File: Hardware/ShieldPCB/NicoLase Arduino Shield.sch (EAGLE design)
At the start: 17 parts, among them IC1 4050D, J1 ARDUINO_R3_SHIELD, U1 7432SE

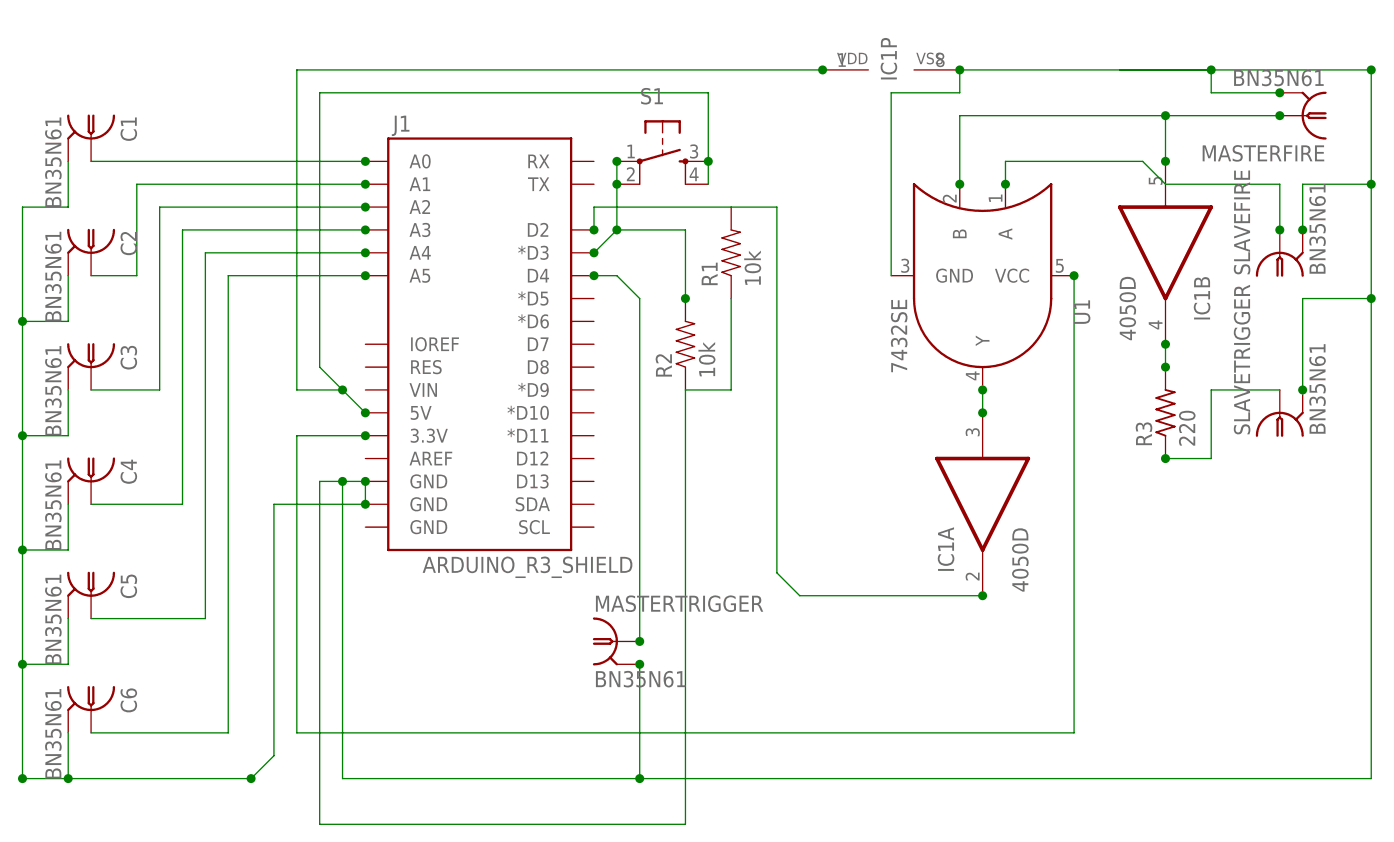
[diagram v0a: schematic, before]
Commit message: Updated PCB to include pull-down resistors on both inputs of OR gate.
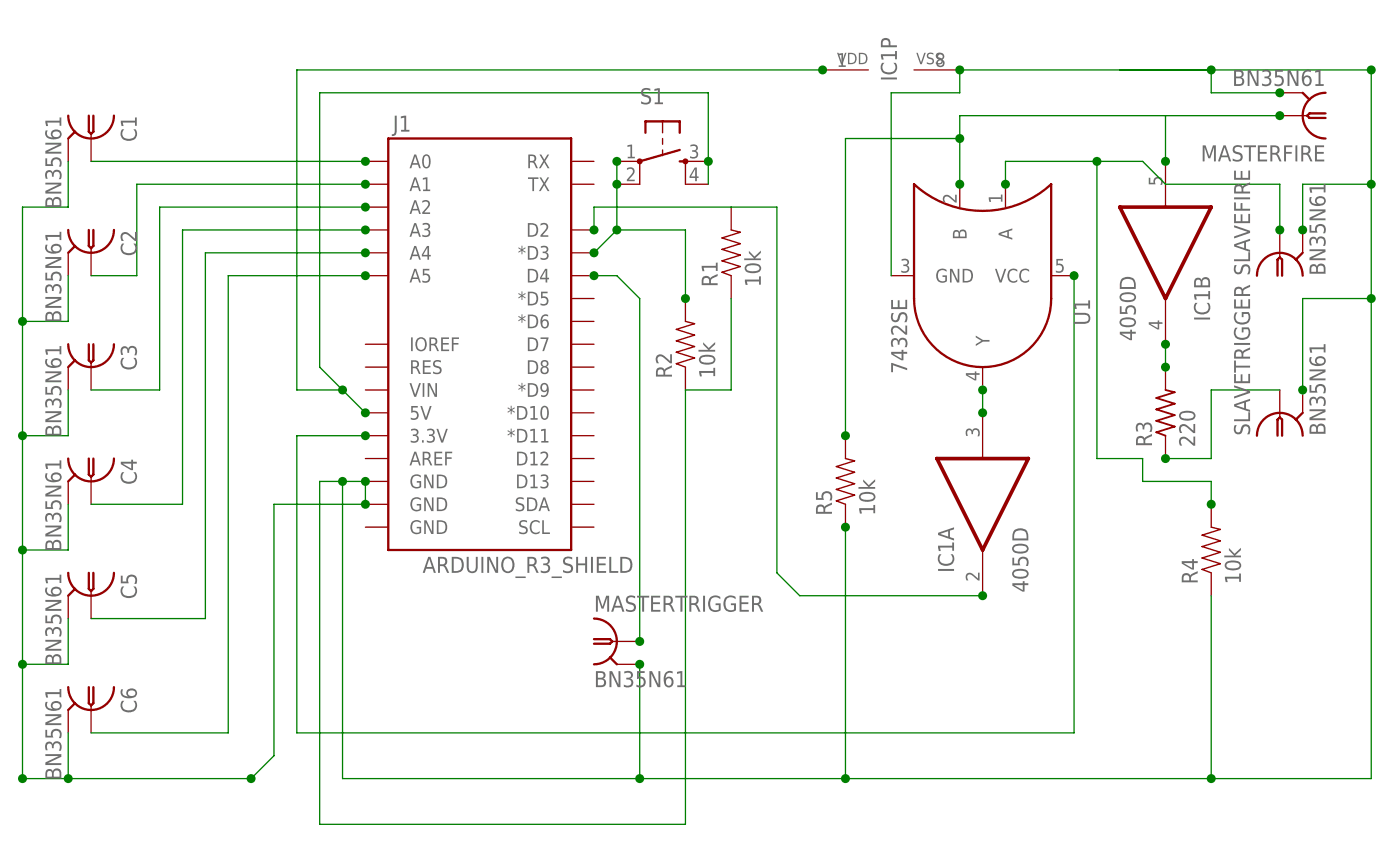
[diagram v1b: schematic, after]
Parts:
- added R4, R5: 10k, SparkFun-Resistors:RESISTOR1206
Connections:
- removed net N$14: SLAVEFIRE.1, U1.A
- new net N$26: R4.2, SLAVEFIRE.1, U1.A
- net N$2: now also R4.1, R5.1
- net SLAVEFIRE: now also R5.2
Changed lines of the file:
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@@
 <part name="MASTERTRIGGER" library="con-coax" deviceset="BN35N61" device=""/>
 <part name="J1" library="SparkFun-Boards" deviceset="ARDUINO_R3_SHIELD" device=""/>
+<part name="R4" library="SparkFun-Resistors" deviceset="RESISTOR" device="1206" value="10k"/>
+<part name="R5" library="SparkFun-Resistors" deviceset="RESISTOR" device="1206" value="10k"/>
 </parts>
 <sheets>
@@
 <instance part="MASTERTRIGGER" gate="G$1" x="76.2" y="27.94"/>
 <instance part="J1" gate="G$1" x="60.96" y="63.5"/>
+<instance part="R4" gate="G$1" x="142.24" y="38.1" rot="R90"/>
+<instance part="R5" gate="G$1" x="101.6" y="45.72" rot="R90"/>
 </instances>
 <busses>
@@
 <net name="SLAVEFIRE" class="0">
 <segment>
+<pinref part="U1" gate="G$1" pin="B"/>
+<wire x1="137.16" y1="86.36" x2="114.3" y2="86.36" width="0.1524" layer="91"/>
+<wire x1="114.3" y1="86.36" x2="114.3" y2="83.82" width="0.1524" layer="91"/>
+<junction x="114.3" y="78.74"/>
+<wire x1="114.3" y1="83.82" x2="114.3" y2="78.74" width="0.1524" layer="91"/>
+<wire x1="114.3" y1="83.82" x2="101.6" y2="83.82" width="0.1524" layer="91"/>
+<pinref part="R5" gate="G$1" pin="2"/>
+<wire x1="101.6" y1="83.82" x2="101.6" y2="50.8" width="0.1524" layer="91"/>
+<junction x="114.3" y="83.82"/>
+<junction x="101.6" y="50.8"/>
 <pinref part="MASTERFIRE" gate="G$1" pin="1"/>
 <junction x="149.86" y="86.36"/>
 <wire x1="149.86" y1="86.36" x2="137.16" y2="86.36" width="0.1524" layer="91"/>
-<pinref part="U1" gate="G$1" pin="B"/>
-<wire x1="137.16" y1="86.36" x2="114.3" y2="86.36" width="0.1524" layer="91"/>
-<wire x1="114.3" y1="86.36" x2="114.3" y2="78.74" width="0.1524" layer="91"/>
-<junction x="114.3" y="78.74"/>
 <pinref part="IC1" gate="B" pin="I"/>
 <wire x1="137.16" y1="81.28" x2="137.16" y2="86.36" width="0.1524" layer="91"/>
 <junction x="137.16" y="81.28"/>
-<junction x="137.16" y="86.36"/>
 </segment>
 </net>
@@
 <wire x1="45.72" y1="45.72" x2="45.72" y2="12.7" width="0.1524" layer="91"/>
 <wire x1="45.72" y1="12.7" x2="78.74" y2="12.7" width="0.1524" layer="91"/>
-<wire x1="78.74" y1="12.7" x2="160.02" y2="12.7" width="0.1524" layer="91"/>
+<wire x1="78.74" y1="12.7" x2="101.6" y2="12.7" width="0.1524" layer="91"/>
+<wire x1="101.6" y1="12.7" x2="142.24" y2="12.7" width="0.1524" layer="91"/>
+<wire x1="142.24" y1="12.7" x2="160.02" y2="12.7" width="0.1524" layer="91"/>
 <wire x1="160.02" y1="12.7" x2="160.02" y2="66.04" width="0.1524" layer="91"/>
 <wire x1="160.02" y1="91.44" x2="142.24" y2="91.44" width="0.1524" layer="91"/>
@@
 <pinref part="J1" gate="G$1" pin="GND@1"/>
 <junction x="48.26" y="43.18"/>
+<pinref part="R5" gate="G$1" pin="1"/>
+<wire x1="101.6" y1="40.64" x2="101.6" y2="12.7" width="0.1524" layer="91"/>
+<pinref part="R4" gate="G$1" pin="1"/>
+<wire x1="142.24" y1="33.02" x2="142.24" y2="12.7" width="0.1524" layer="91"/>
+<junction x="101.6" y="40.64"/>
+<junction x="101.6" y="12.7"/>
+<junction x="142.24" y="12.7"/>
 </segment>
 </net>
@@
 <wire x1="40.64" y1="50.8" x2="48.26" y2="50.8" width="0.1524" layer="91"/>
 <junction x="48.26" y="50.8"/>
-</segment>
-</net>
-<net name="N$14" class="0">
-<segment>
-<pinref part="SLAVEFIRE" gate="G$1" pin="1"/>
-<junction x="149.86" y="73.66"/>
-<wire x1="149.86" y1="73.66" x2="149.86" y2="78.74" width="0.1524" layer="91"/>
-<wire x1="149.86" y1="78.74" x2="137.16" y2="78.74" width="0.1524" layer="91"/>
-<wire x1="137.16" y1="78.74" x2="134.62" y2="81.28" width="0.1524" layer="91"/>
-<wire x1="134.62" y1="81.28" x2="119.38" y2="81.28" width="0.1524" layer="91"/>
-<pinref part="U1" gate="G$1" pin="A"/>
-<wire x1="119.38" y1="81.28" x2="119.38" y2="78.74" width="0.1524" layer="91"/>
-<junction x="119.38" y="78.74"/>
 </segment>
 </net>
@@
 </segment>
 </net>
+<net name="N$26" class="0">
+<segment>
+<pinref part="R4" gate="G$1" pin="2"/>
+<junction x="142.24" y="43.18"/>
+<wire x1="142.24" y1="45.72" x2="142.24" y2="43.18" width="0.1524" layer="91"/>
+<wire x1="134.62" y1="45.72" x2="142.24" y2="45.72" width="0.1524" layer="91"/>
+<wire x1="134.62" y1="48.26" x2="134.62" y2="45.72" width="0.1524" layer="91"/>
+<wire x1="129.54" y1="48.26" x2="134.62" y2="48.26" width="0.1524" layer="91"/>
+<pinref part="SLAVEFIRE" gate="G$1" pin="1"/>
+<junction x="149.86" y="73.66"/>
+<wire x1="149.86" y1="73.66" x2="149.86" y2="78.74" width="0.1524" layer="91"/>
+<wire x1="149.86" y1="78.74" x2="137.16" y2="78.74" width="0.1524" layer="91"/>
+<wire x1="137.16" y1="78.74" x2="134.62" y2="81.28" width="0.1524" layer="91"/>
+<wire x1="134.62" y1="81.28" x2="129.54" y2="81.28" width="0.1524" layer="91"/>
+<pinref part="U1" gate="G$1" pin="A"/>
+<wire x1="129.54" y1="81.28" x2="119.38" y2="81.28" width="0.1524" layer="91"/>
+<wire x1="119.38" y1="81.28" x2="119.38" y2="78.74" width="0.1524" layer="91"/>
+<junction x="119.38" y="78.74"/>
+<wire x1="129.54" y1="48.26" x2="129.54" y2="81.28" width="0.1524" layer="91"/>
+<junction x="129.54" y="81.28"/>
+</segment>
+</net>
